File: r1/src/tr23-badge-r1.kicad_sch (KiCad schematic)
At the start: 58 parts, among them Q1 MMBT3904-TP, Q2 MMBT3904-TP, Q3 MMBT3904-TP, Y1 32.768kHz

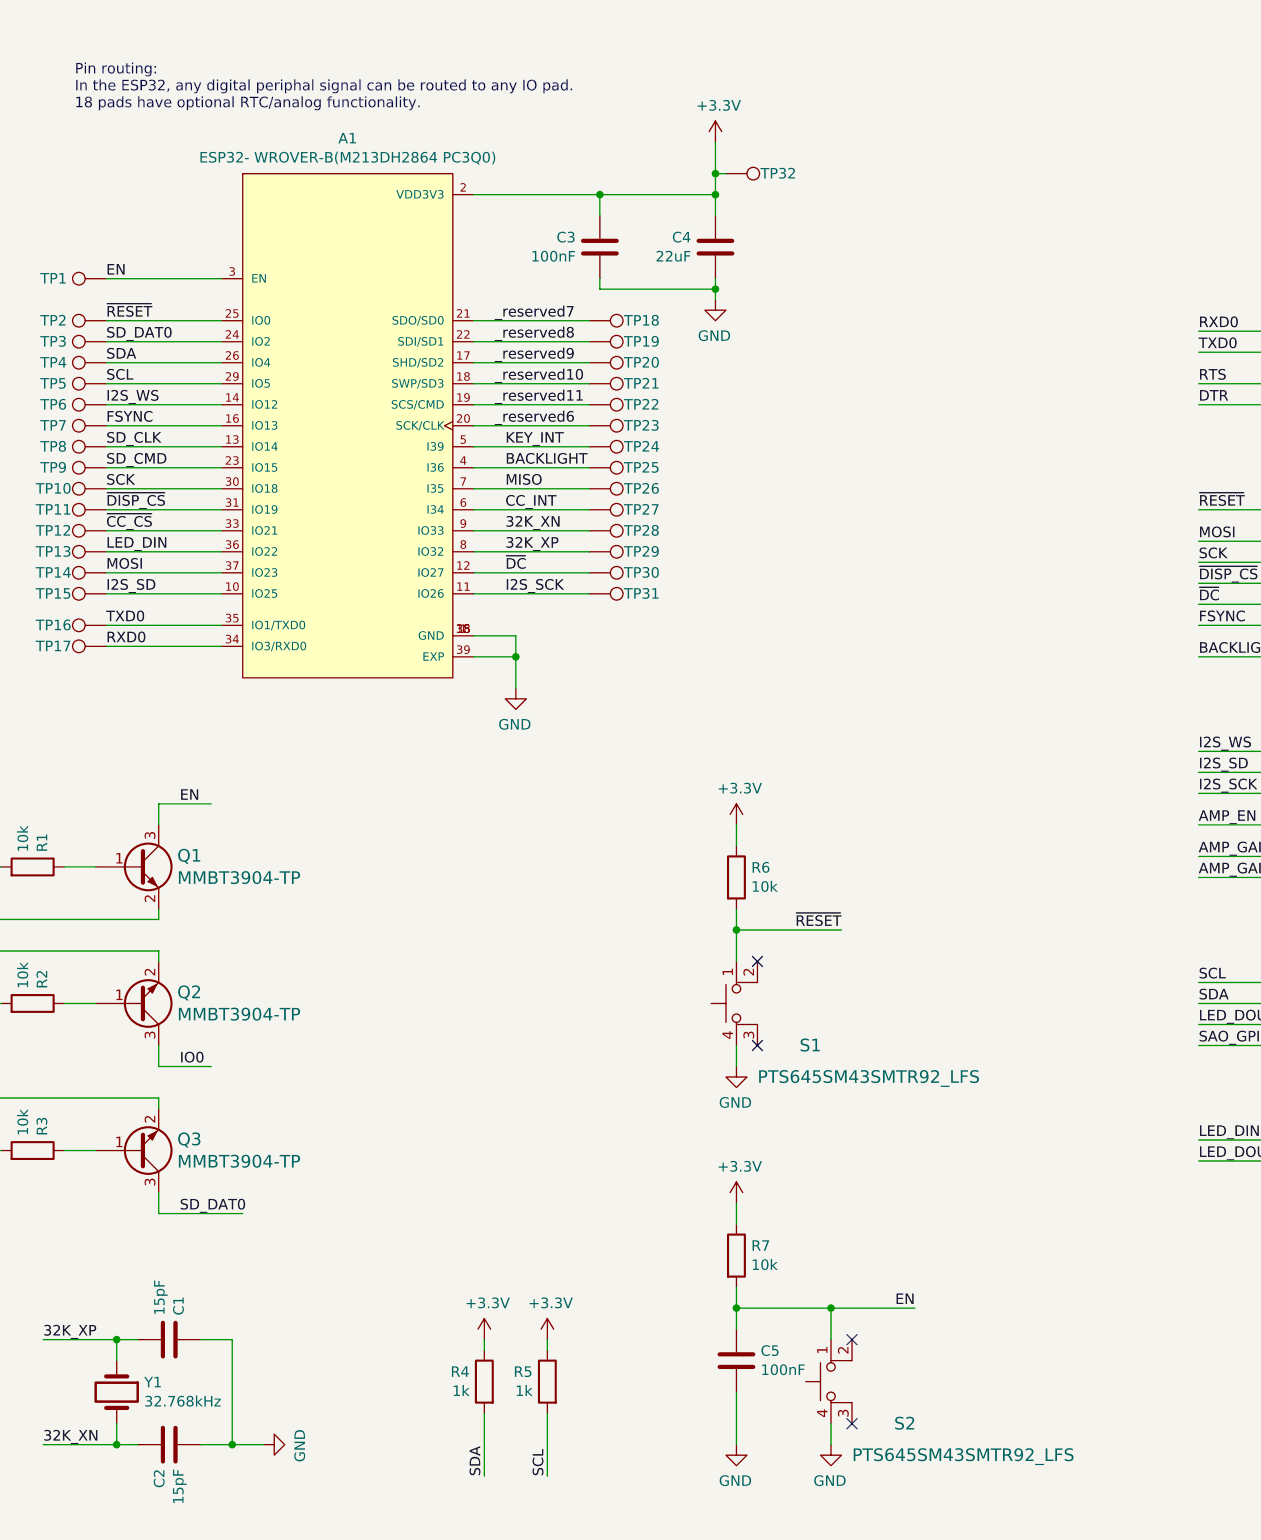
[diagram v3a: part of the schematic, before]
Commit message: Assign MPN's and LCSC part numbers
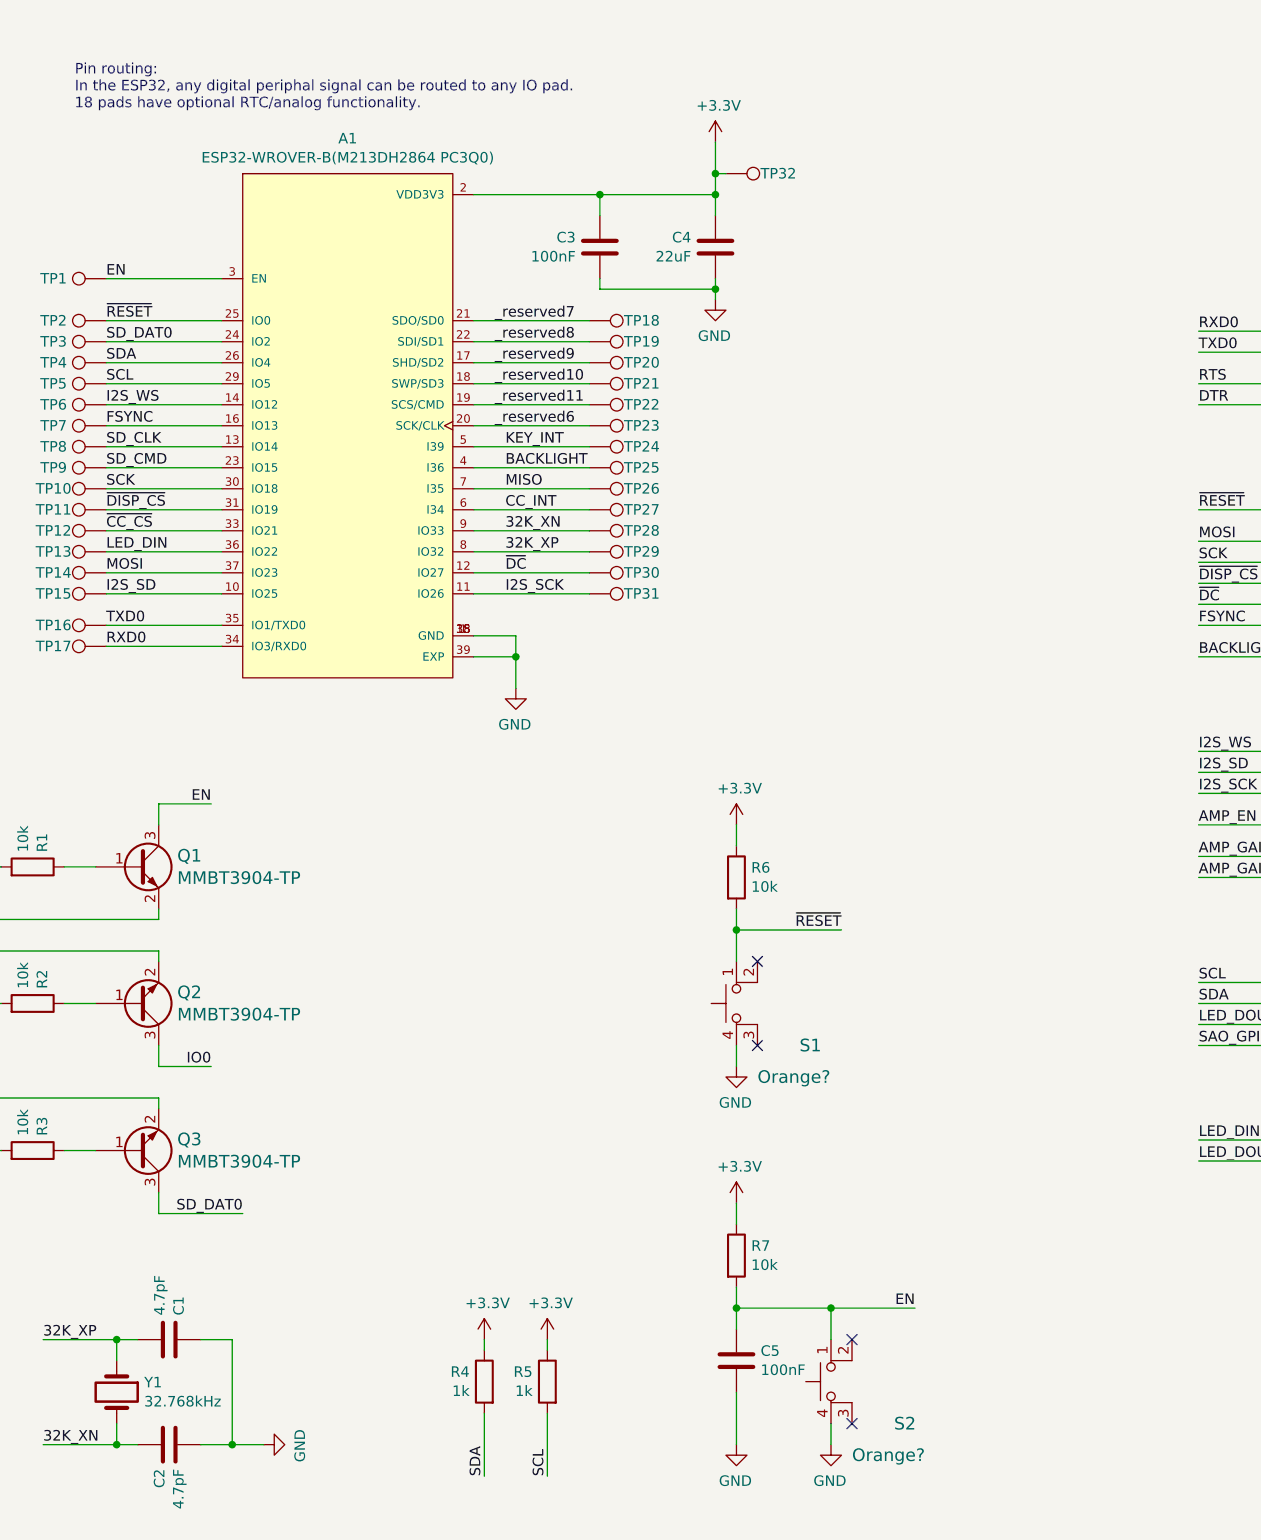
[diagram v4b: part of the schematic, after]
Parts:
- A1: value ESP32- WROVER-B(M213DH2864 PC3Q0) -> ESP32-WROVER-B(M213DH2864 PC3Q0); Field5 ESP32-WROVER-I -> (none); LCSC (none) -> C503591; MPN (none) -> ESP32-WROVER-B
- C1, C2: value 15pF -> 4.7pF; Tempco (none) -> C0G
- Q1, Q2, Q3: LCSC (none) -> C909754
- S1, S2: value PTS645SM43SMTR92_LFS -> Orange?; MPN PTS645SM43SMTR92 LFS -> (none)
- Y1: LCSC (none) -> C48615; MPN SSP-T7-F -> Q13FC1350000200
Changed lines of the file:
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@@
     (effects (font (size 1.27 1.27)) (justify left bottom))
   )
-  (label "EN" (at 60.96 107.95 0) (fields_autoplaced)
-    (effects (font (size 1.27 1.27)) (justify left bottom))
+  (label "EN" (at 64.77 107.95 180) (fields_autoplaced)
+    (effects (font (size 1.27 1.27)) (justify right bottom))
   )
   (label "CC_RESET" (at 231.14 64.77 0) (fields_autoplaced)
@@
     (effects (font (size 1.27 1.27)) (justify right bottom))
   )
-  (label "IO0" (at 60.96 139.7 0) (fields_autoplaced)
-    (effects (font (size 1.27 1.27)) (justify left bottom))
+  (label "IO0" (at 64.77 139.7 180) (fields_autoplaced)
+    (effects (font (size 1.27 1.27)) (justify right bottom))
   )
   (label "SCL" (at 52.07 57.15 0) (fields_autoplaced)
@@
     (effects (font (size 1.27 1.27)) (justify left bottom))
   )
-  (label "SD_DAT0" (at 60.96 157.48 0) (fields_autoplaced)
-    (effects (font (size 1.27 1.27)) (justify left bottom))
+  (label "SD_DAT0" (at 68.58 157.48 180) (fields_autoplaced)
+    (effects (font (size 1.27 1.27)) (justify right bottom))
   )
   (label "RXD0" (at 52.07 88.9 0) (fields_autoplaced)
@@
       (effects (font (size 1.27 1.27)))
     )
-    (property "Value" "ESP32- WROVER-B(M213DH2864 PC3Q0)" (at 81.28 29.8196 0)
+    (property "Value" "ESP32-WROVER-B(M213DH2864 PC3Q0)" (at 81.28 29.8196 0)
       (effects (font (size 1.27 1.27)))
     )
@@
       (effects (font (size 1.27 1.27)) (justify left bottom) hide)
     )
-    (property "Field5" "ESP32-WROVER-I" (at 81.28 62.23 0)
+    (property "MPN" "ESP32-WROVER-B" (at 81.28 62.23 0)
       (effects (font (size 1.27 1.27)) (justify left bottom) hide)
     )
@@
     (property "Field8" "1904-1008-1-ND" (at 81.28 62.23 0)
       (effects (font (size 1.27 1.27)) (justify left bottom) hide)
+    )
+    (property "LCSC" "C503591" (at 81.28 62.23 0)
+      (effects (font (size 1.27 1.27)) hide)
     )
     (pin "1")
@@
       (effects (font (size 1.524 1.524)) (justify left) hide)
     )
+    (property "LCSC" "C909754" (at 55.88 115.57 0)
+      (effects (font (size 1.27 1.27)) hide)
+    )
     (pin "1")
     (pin "2")
@@
       (effects (font (size 1.524 1.524)) (justify left) hide)
     )
+    (property "LCSC" "C909754" (at 55.88 132.08 0)
+      (effects (font (size 1.27 1.27)) hide)
+    )
     (pin "1")
     (pin "2")
@@
       (effects (font (size 1.27 1.27)) hide)
     )
-    (property "MPN" "SSP-T7-F" (at 53.34 179.07 90)
+    (property "MPN" "Q13FC1350000200" (at 53.34 179.07 90)
+      (effects (font (size 1.27 1.27)) hide)
+    )
+    (property "LCSC" "C48615" (at 53.34 179.07 90)
       (effects (font (size 1.27 1.27)) hide)
     )
@@
       (effects (font (size 1.27 1.27)) (justify left))
     )
-    (property "Value" "15pF" (at 58.547 169.799 0)
+    (property "Value" "4.7pF" (at 58.547 169.799 0)
       (effects (font (size 1.27 1.27)) (justify left))
     )
@@
     )
     (property "Datasheet" "~" (at 59.69 172.72 0)
+      (effects (font (size 1.27 1.27)) hide)
+    )
+    (property "Tempco" "C0G" (at 59.69 172.72 0)
       (effects (font (size 1.27 1.27)) hide)
     )
@@
       (effects (font (size 1.524 1.524)) (justify left) hide)
     )
+    (property "LCSC" "C909754" (at 55.88 149.86 0)
+      (effects (font (size 1.27 1.27)) hide)
+    )
     (pin "1")
     (pin "2")
@@
       (effects (font (size 1.524 1.524)) (justify right))
     )
-    (property "Value" "PTS645SM43SMTR92_LFS" (at 130.81 140.97 90)
+    (property "Value" "Orange?" (at 130.81 140.97 90)
       (effects (font (size 1.524 1.524)) (justify right))
     )
@@
       (effects (font (size 1.524 1.524)) (justify left) hide)
     )
-    (property "MPN" "PTS645SM43SMTR92 LFS" (at 118.11 137.16 0)
+    (property "MPN" "" (at 118.11 137.16 0)
       (effects (font (size 1.524 1.524)) (justify left) hide)
     )
@@
       (effects (font (size 1.524 1.524)) (justify right))
     )
-    (property "Value" "PTS645SM43SMTR92_LFS" (at 142.24 186.69 90)
+    (property "Value" "Orange?" (at 142.24 186.69 90)
       (effects (font (size 1.524 1.524)) (justify right))
     )
@@
       (effects (font (size 1.524 1.524)) (justify left) hide)
     )
-    (property "MPN" "PTS645SM43SMTR92 LFS" (at 129.54 182.88 0)
+    (property "MPN" "" (at 129.54 182.88 0)
       (effects (font (size 1.524 1.524)) (justify left) hide)
     )
@@
       (effects (font (size 1.27 1.27)) (justify left))
     )
-    (property "Value" "15pF" (at 60.833 188.341 0)
+    (property "Value" "4.7pF" (at 60.833 188.341 0)
       (effects (font (size 1.27 1.27)) (justify left))
     )
@@
       (effects (font (size 1.27 1.27)) hide)
     )
+    (property "Tempco" "C0G" (at 59.69 185.42 0)
+      (effects (font (size 1.27 1.27)) hide)
+    )

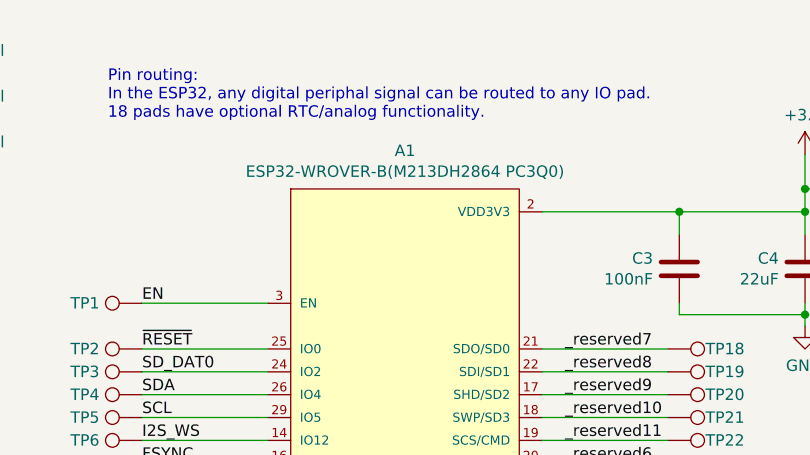
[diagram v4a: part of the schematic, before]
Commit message: Assign manufacturers
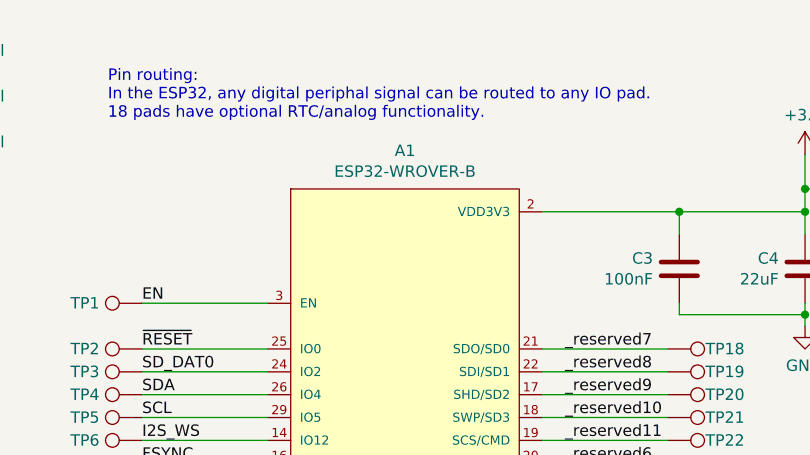
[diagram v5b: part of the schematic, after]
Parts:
- A1: value ESP32-WROVER-B(M213DH2864 PC3Q0) -> ESP32-WROVER-B; Field7 Espressif Systems -> (none); Manufacturer (none) -> Espressif
- Y1: Manufacturer (none) -> Seiko Epson
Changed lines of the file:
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@@
       (effects (font (size 1.27 1.27)))
     )
-    (property "Value" "ESP32-WROVER-B(M213DH2864 PC3Q0)" (at 81.28 29.8196 0)
+    (property "Value" "ESP32-WROVER-B" (at 81.28 29.8196 0)
       (effects (font (size 1.27 1.27)))
     )
@@
       (effects (font (size 1.27 1.27)) (justify left bottom) hide)
     )
-    (property "Field7" "Espressif Systems" (at 81.28 62.23 0)
+    (property "Manufacturer" "Espressif" (at 81.28 62.23 0)
       (effects (font (size 1.27 1.27)) (justify left bottom) hide)
     )
@@
       (effects (font (size 1.27 1.27)) hide)
     )
+    (property "Manufacturer" "Seiko Epson" (at 53.34 179.07 90)
+      (effects (font (size 1.27 1.27)) hide)
+    )

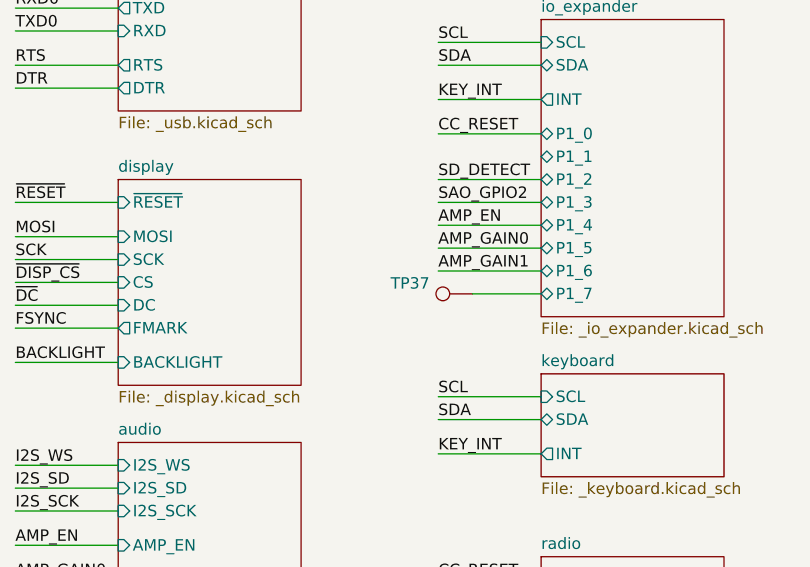
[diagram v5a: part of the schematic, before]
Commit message: Reannotate component refs
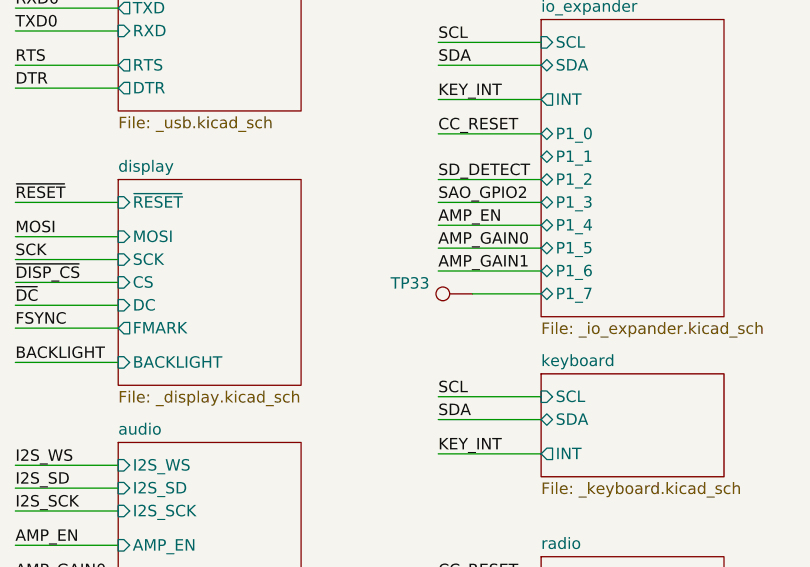
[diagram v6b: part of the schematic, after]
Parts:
- renumbered TP37 to TP33
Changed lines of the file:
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@@
   (symbol (lib_id "Connector:TestPoint") (at 234.95 82.55 90) (mirror x) (unit 1)
     (in_bom yes) (on_board yes) (dnp no)
-    (property "Reference" "TP37" (at 230.1748 81.3816 90)
+    (property "Reference" "TP33" (at 230.1748 81.3816 90)
       (effects (font (size 1.27 1.27)) (justify left))
     )
@@
       (project "tr23-badge-r1"
         (path "/ab725fe7-4504-40ef-b6af-82d065d00fb6"
-          (reference "TP37") (unit 1)
+          (reference "TP33") (unit 1)
         )
       )
